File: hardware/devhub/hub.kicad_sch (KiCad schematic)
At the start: 36 parts, among them J2 USB-C UPSTREAM, J3 PORTA 7 (scorta), U12 MCP120T-300I/TT, U2 USB2517I-JZX, Y1 24MHz 12pF

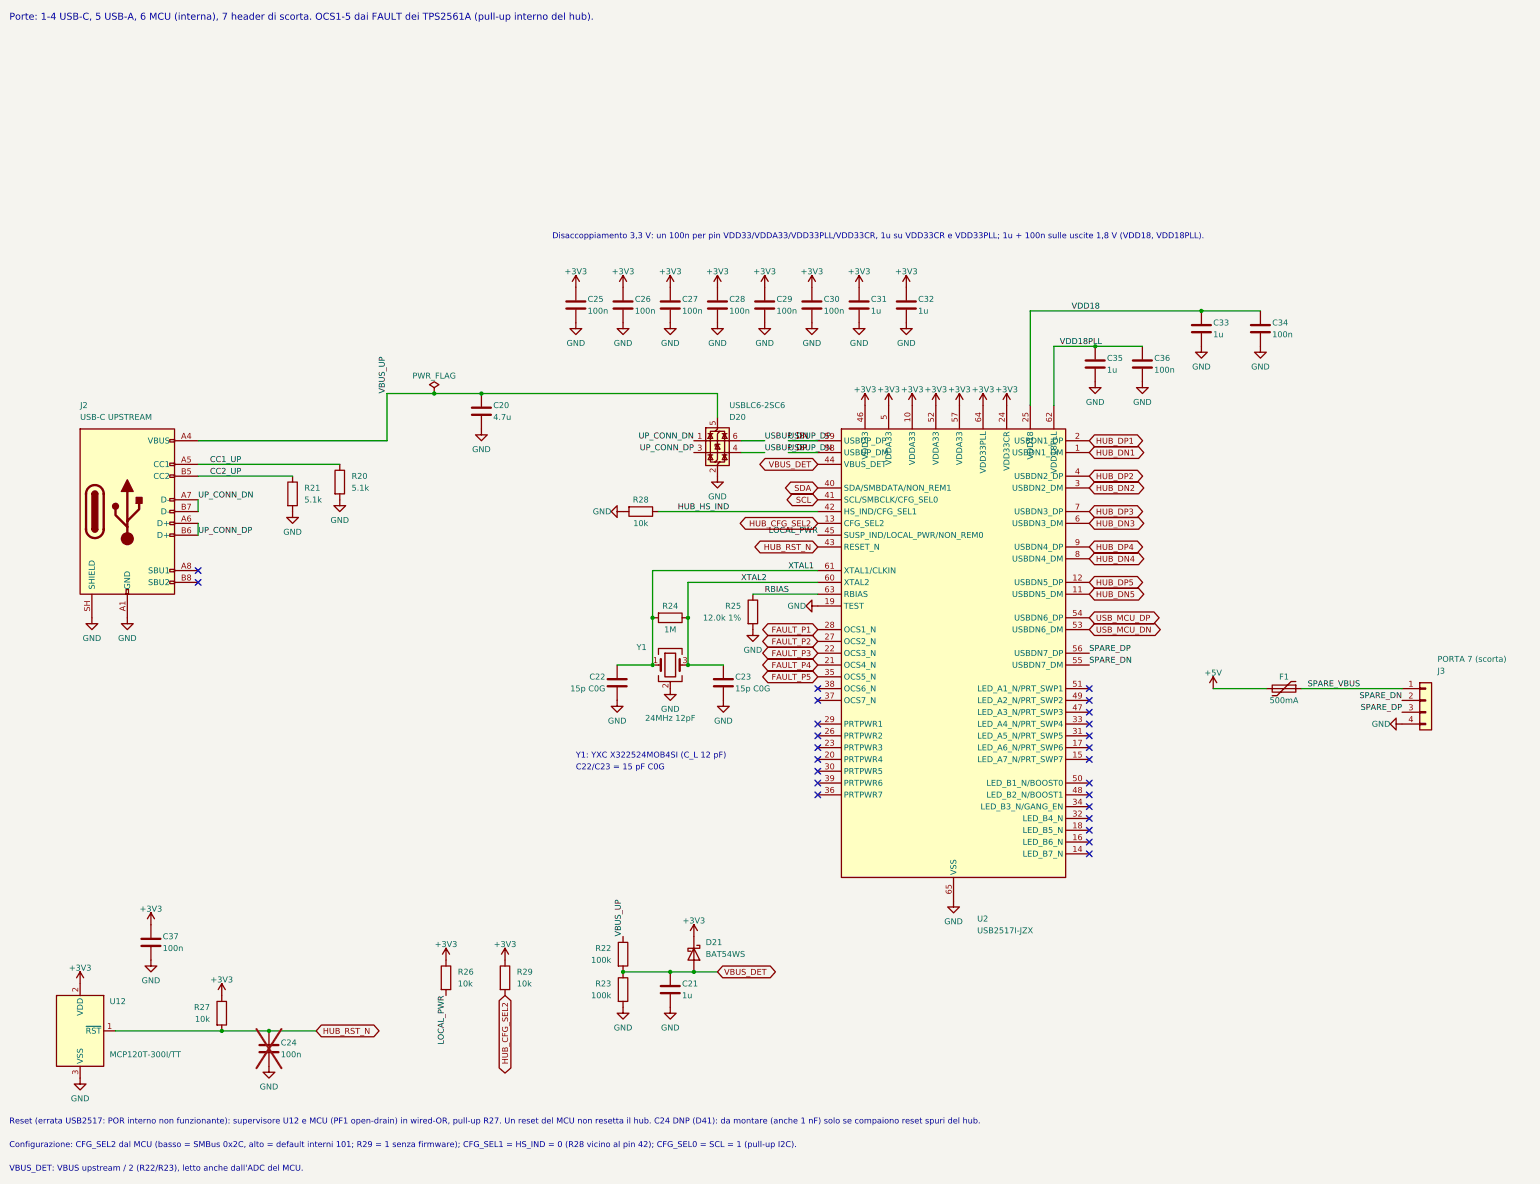
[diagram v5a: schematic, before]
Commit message: MCU and hub decoupling, USB2517 checklist, VBUS_DET without clamp diode (D53, D57, D58)
- MCU U3 decoupling per DS13560 fig. 15: C41 100 nF + C40 4.7 uF on VDD/VSS,
  C42 100 nF on VREF+; C43, C44 and C45 removed (D57).
- Hub U2 decoupling per the Microchip USB2517 Hardware Design Checklist: 100 nF on
  each 3.3 V pin (C38 added), 1 uF shared by VDDA33 (C31) and on VDD33CR, only 1 uF
  on VDD18 and VDD18PLL (C34, C36 removed). Each capacitor drawn on its pin's wire.
  The 100 nF of U2 and U12 are 0402 (stock ID 217) to fit next to the pins between
  the USB pairs; DRC exception for the +3V3 stubs inside the U2_DECAP areas (D58).
- VBUS_DET: D21 removed, plain 100k/100k divider as recommended by the checklist
  (D53, R03-02 closed).
- USB-C connector exits without tuning meanders: the ~2.3 mm D+/D- difference of the
  pad crossing is accepted; looser skew limit on the connector-side nets.
- PCB: relay contact keepouts redrawn, U2 fanout and decoupling placement, zone refill.
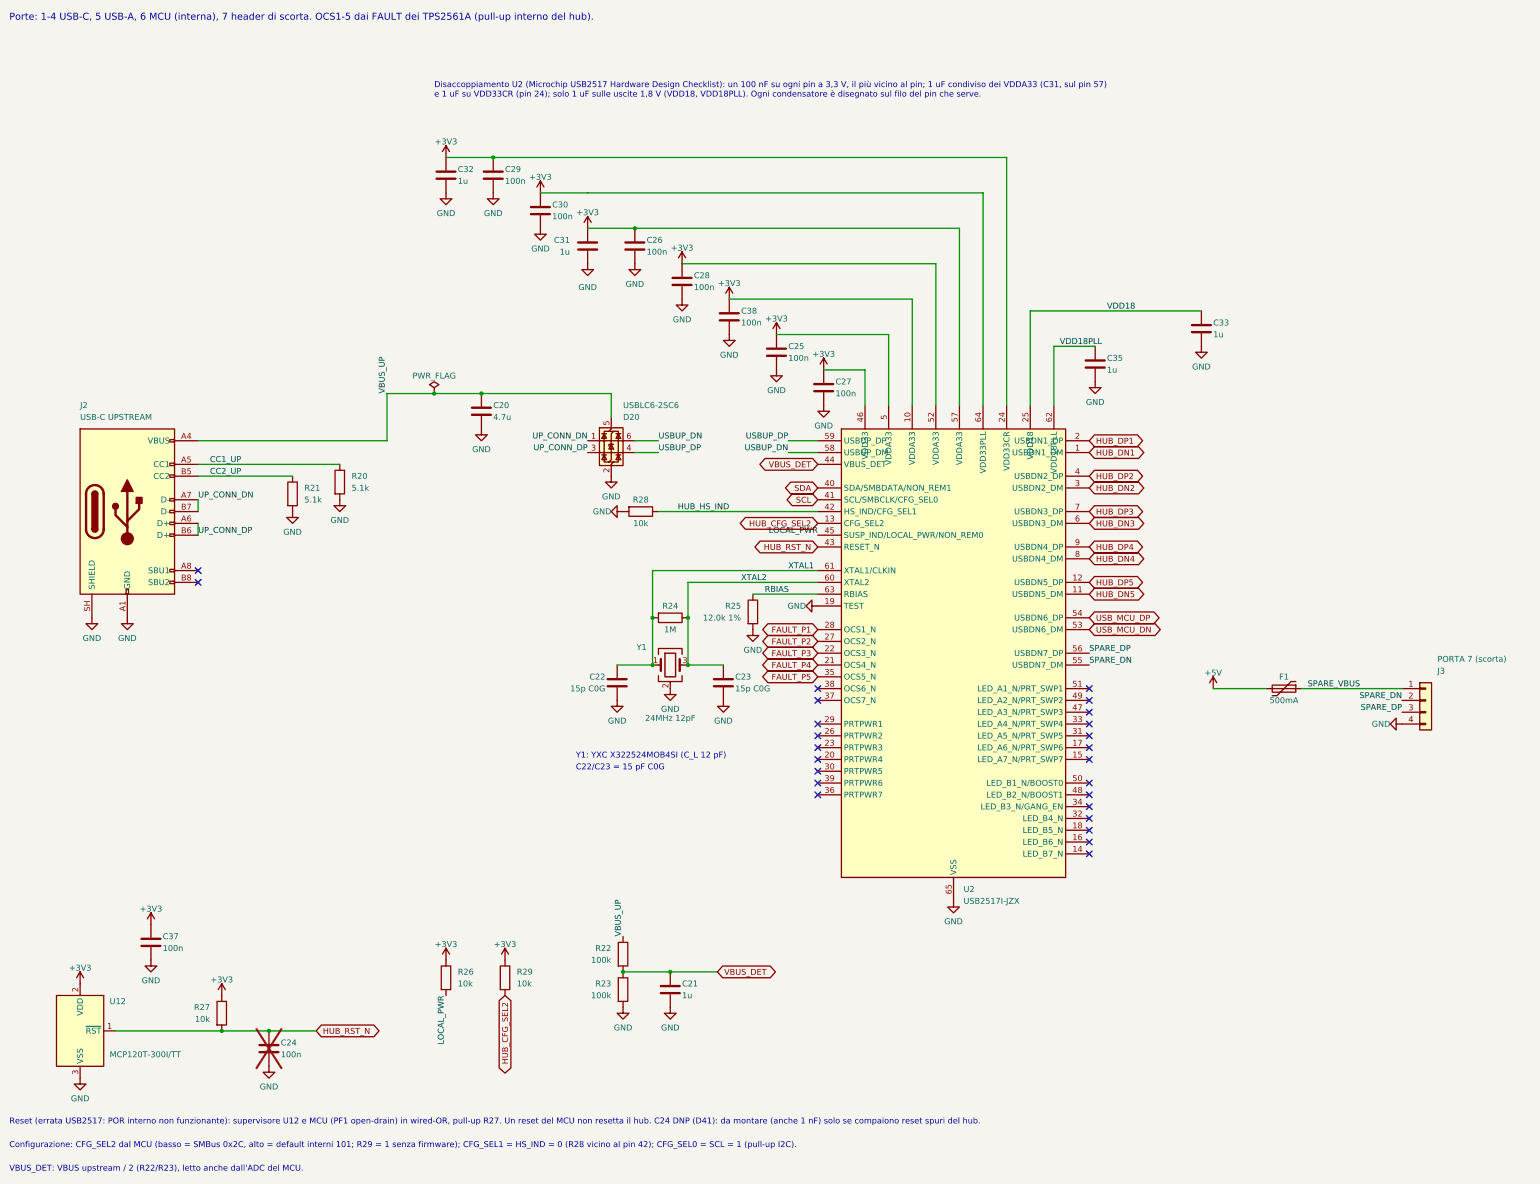
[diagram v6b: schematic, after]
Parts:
- removed C34, C36: 100n, Capacitor_SMD:C_0603_1608Metric, symbol Device:C
- removed D21: BAT54WS, Diode_SMD:D_SOD-323, symbol Device:D_Schottky
- added C38: 100n, Capacitor_SMD:C_0402_1005Metric, symbol Device:C
- C25, C26, C27, C28, C29, C30, C37: footprint Capacitor_SMD:C_0603_1608Metric -> Capacitor_SMD:C_0402_1005Metric; digikey 1276-1000-1-ND -> 311-1338-1-ND; lcsc C1591 -> C60474; mouser 187-CL10B104KB8NNNC -> 603-CC402KRX7R7BB104; warehouse 235 -> 217
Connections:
- net +3V3: now also C38.1
- net GND: now also C38.2
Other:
- note added: "Disaccoppiamento U2 (Microchip USB2517 Hardware Design Checklist): un 100 nF su ogni pin a 3,3 V, il più vicino al pin; 1 uF condiviso dei VDDA33 (C31, sul pin 57) e 1 uF su VDD33CR (pin 24); solo 1 uF sulle uscite 1,8 V (VDD18, VDD18PLL). Ogni condensatore è disegnato sul filo del pin che serve."
- note removed: "Disaccoppiamento 3,3 V: un 100n per pin VDD33/VDDA33/VDD33PLL/VDD33CR, 1u su VDD33CR e VDD33PLL; 1u + 100n sulle uscite 1,8 V (VDD18, VDD18PLL)."
- moved on the sheet: C25, C26, C27, C28, C29, C30, C31, C32, D20

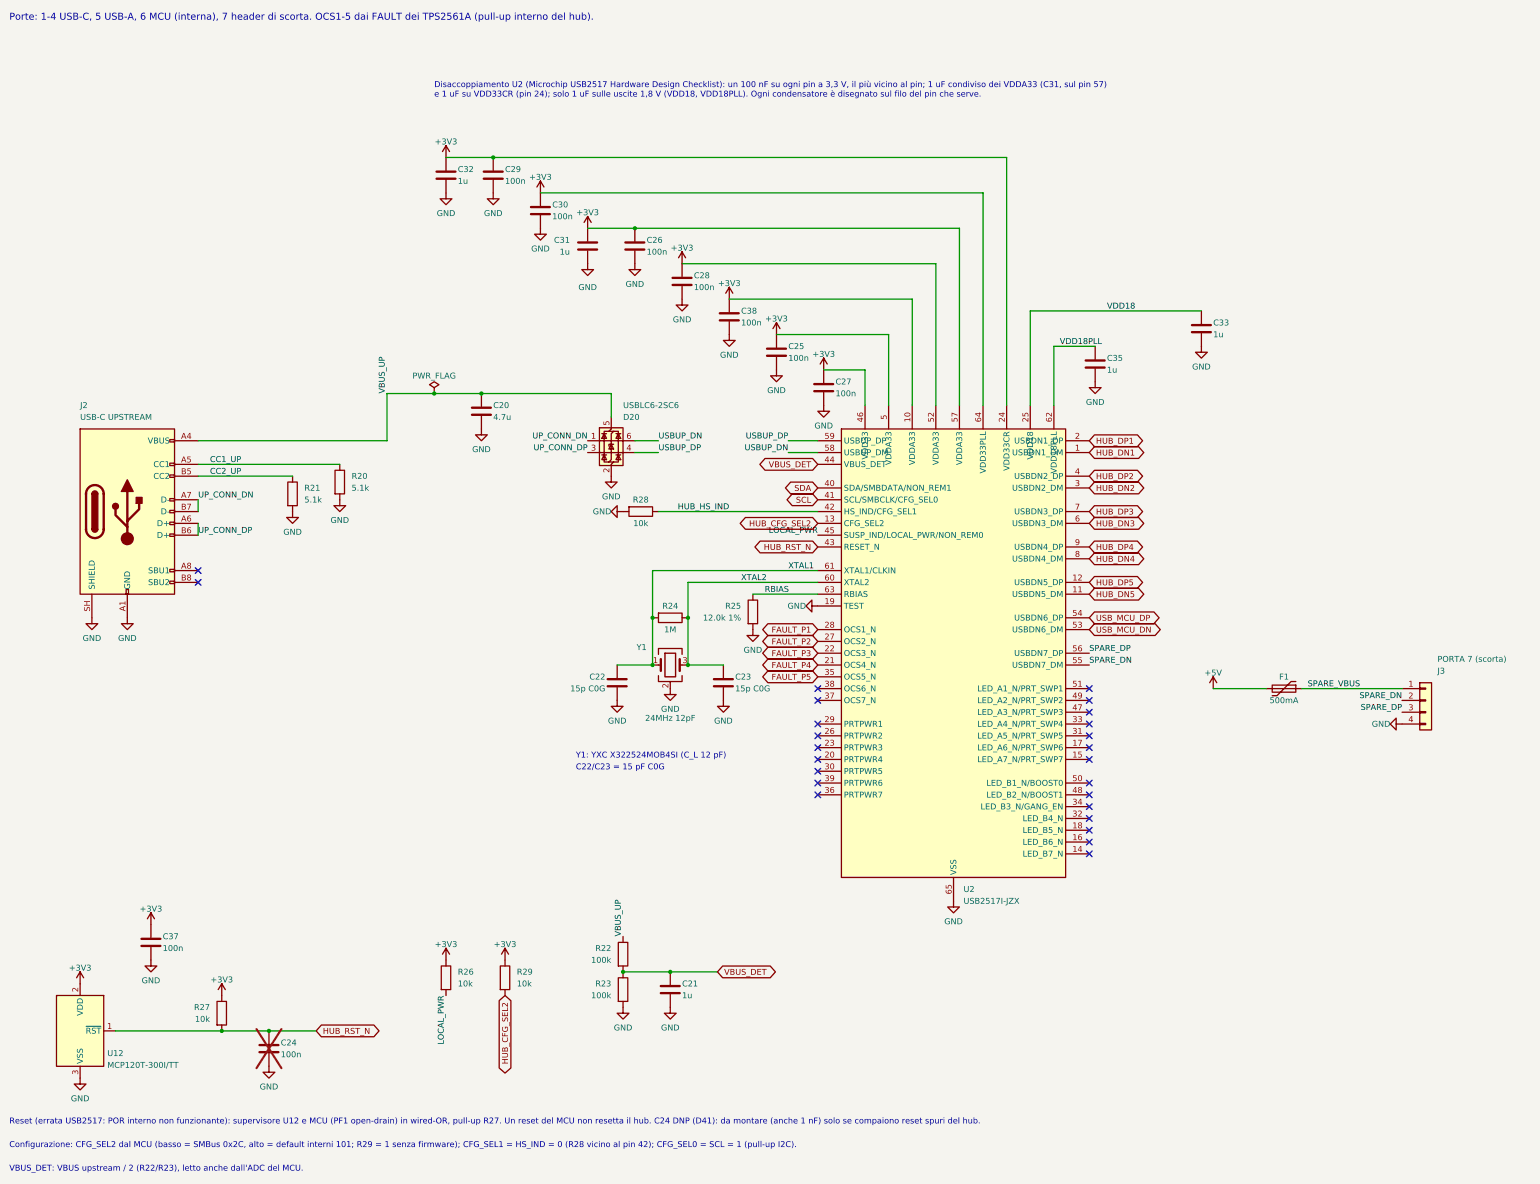
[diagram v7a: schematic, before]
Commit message: Schematic v0.3: apply simplified requirements (D79-D81)
Update the existing KiCad project instead of starting over:
- MCU U3 replaced with STM32G0B1CEU6 (UFQFPN48) on the 48-pin pinout
- switches sheet: two UCS2114-1-V/LX on separate I2C buses replace
  TPS2561A, INA3221 and current shunts
- ports: single MCU-driven LED, discrete VBUS discharge removed
- remove USB-A port, spare hub header, second relay channel,
  input CC ADC filters and input shunt
- add UCS2114 symbol and footprint (Microchip land pattern C04-2421)
- align pinout, decisions, architecture and component docs
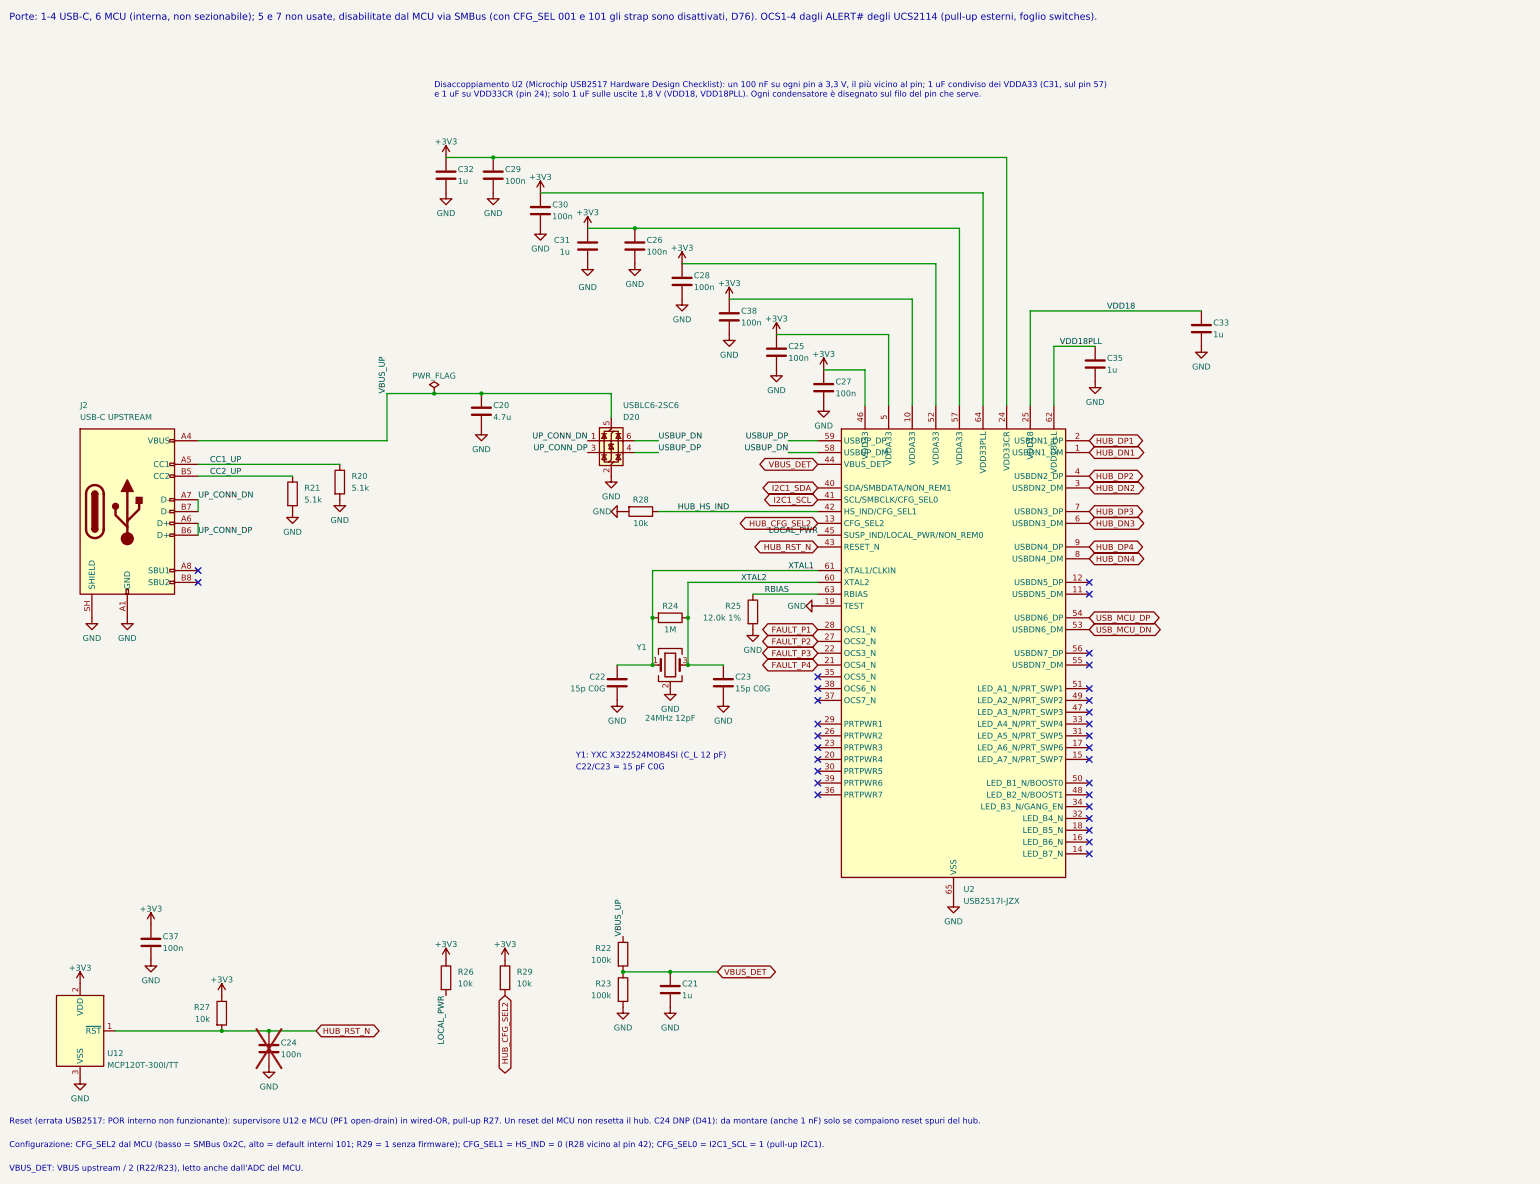
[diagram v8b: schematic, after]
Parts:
- removed F1: 500mA, Fuse:Fuse_1812_4532Metric, symbol Device:Polyfuse
- removed J3: PORTA 7 (scorta), Connector_PinHeader_2.54mm:PinHeader_1x04_P2.54mm_Vertical, symbol Connector_Generic:Conn_01x04
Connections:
- net FAULT_P5: no longer names the net of U2.35 (OCS5_N)
- net HUB_DN5: no longer names the net of U2.11 (USBDN5_DM)
- net HUB_DP5: no longer names the net of U2.12 (USBDN5_DP)
- net SCL renamed I2C1_SCL
- net SDA renamed I2C1_SDA
- net SPARE_DN: no longer names the net of U2.55 (USBDN7_DM)
- net SPARE_DP: no longer names the net of U2.56 (USBDN7_DP)
- no-connect marks 25 -> 30
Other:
- note added: "Configurazione: CFG_SEL2 dal MCU (basso = SMBus 0x2C, alto = default interni 101; R29 = 1 senza firmware); CFG_SEL1 = HS_IND = 0 (R28 vicino al pin 42); CFG_SEL0 = I2C1_SCL = 1 (pull-up I2C1)."
- note added: "Porte: 1-4 USB-C, 6 MCU (interna, non sezionabile); 5 e 7 non usate, disabilitate dal MCU via SMBus (con CFG_SEL 001 e 101 gli strap sono disattivati, D76). OCS1-4 dagli ALERT# degli UCS2114 (pull-up esterni, foglio switches)."
- note removed: "Configurazione: CFG_SEL2 dal MCU (basso = SMBus 0x2C, alto = default interni 101; R29 = 1 senza firmware); CFG_SEL1 = HS_IND = 0 (R28 vicino al pin 42); CFG_SEL0 = SCL = 1 (pull-up I2C)."
- note removed: "Porte: 1-4 USB-C, 5 USB-A, 6 MCU (interna), 7 header di scorta. OCS1-5 dai FAULT dei TPS2561A (pull-up interno del hub)."
